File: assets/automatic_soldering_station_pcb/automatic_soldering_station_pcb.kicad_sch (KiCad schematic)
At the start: 25 parts, among them J1 XY_MOS, J2 MAX6675, J3 MAX6675, J4 MAX6675

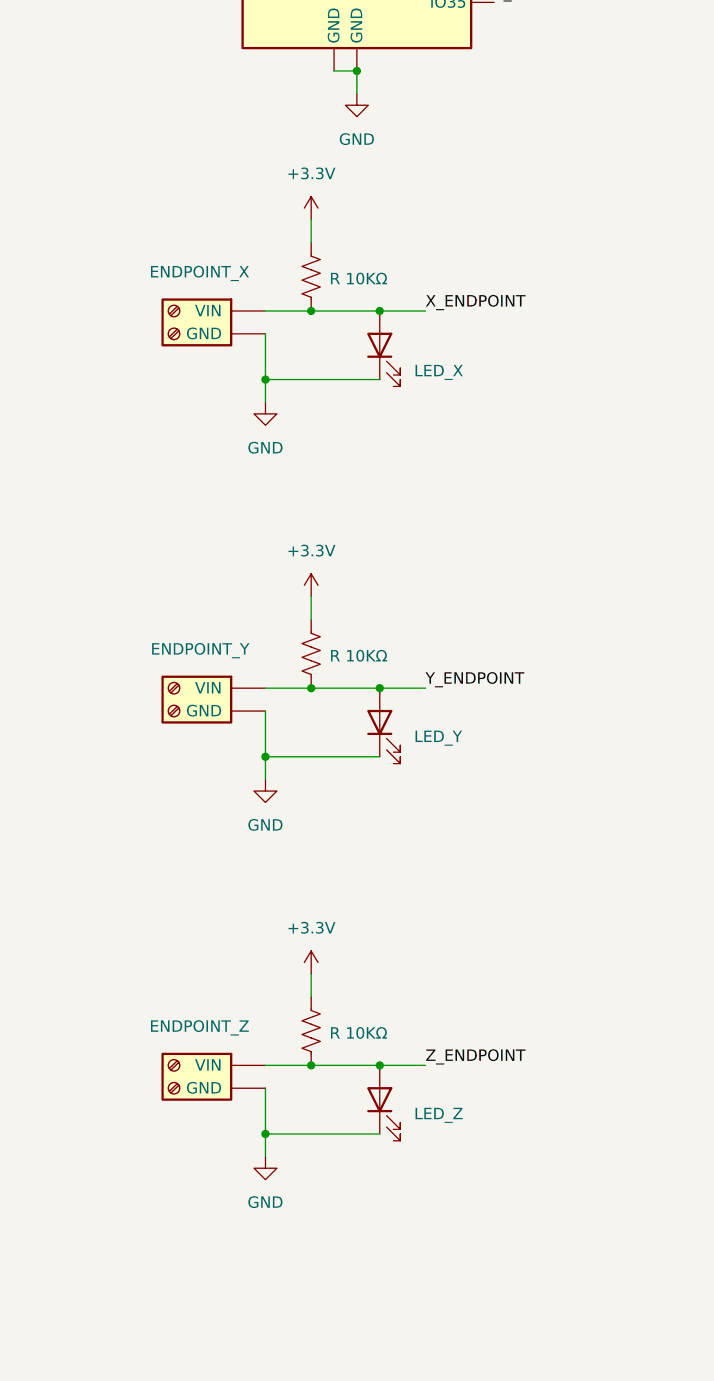
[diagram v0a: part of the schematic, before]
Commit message: pcb: add autorouted results
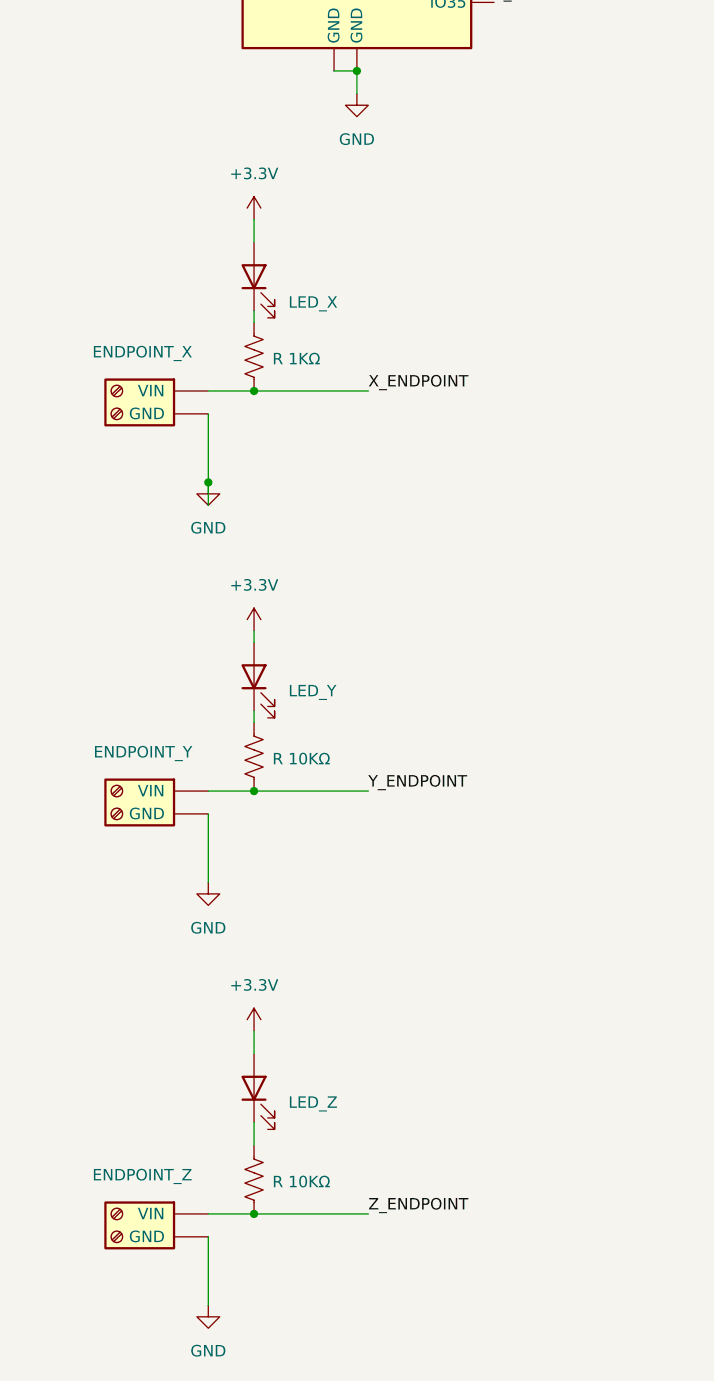
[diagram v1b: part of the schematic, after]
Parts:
- MOTOR_S_CONN1, MOTOR_X_CONN1, MOTOR_Y_CONN1, MOTOR_Z_CONN1: footprint Connector_JST:JST_PH_S4B-PH-K_1x04_P2.00mm_Horizontal -> Connector_JST:JST_PH_B4B-PH-K_1x04_P2.00mm_Vertical
- R1: value R 10KΩ -> R 1KΩ
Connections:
- net +3.3V: now also D1.2 (A), D2.2 (A), D3.2 (A); no longer R1.1, R2.1, R3.1
- net GND: no longer D1.1 (K), D2.1 (K), D3.1 (K)
- net X_ENDPOINT: no longer D1.2 (A)
- net Y_ENDPOINT: no longer D2.2 (A)
- net Z_ENDPOINT: no longer D3.2 (A)
- new net: D2.1 (K), R2.1
- new net: D1.1 (K), R1.1
- new net: D3.1 (K), R3.1

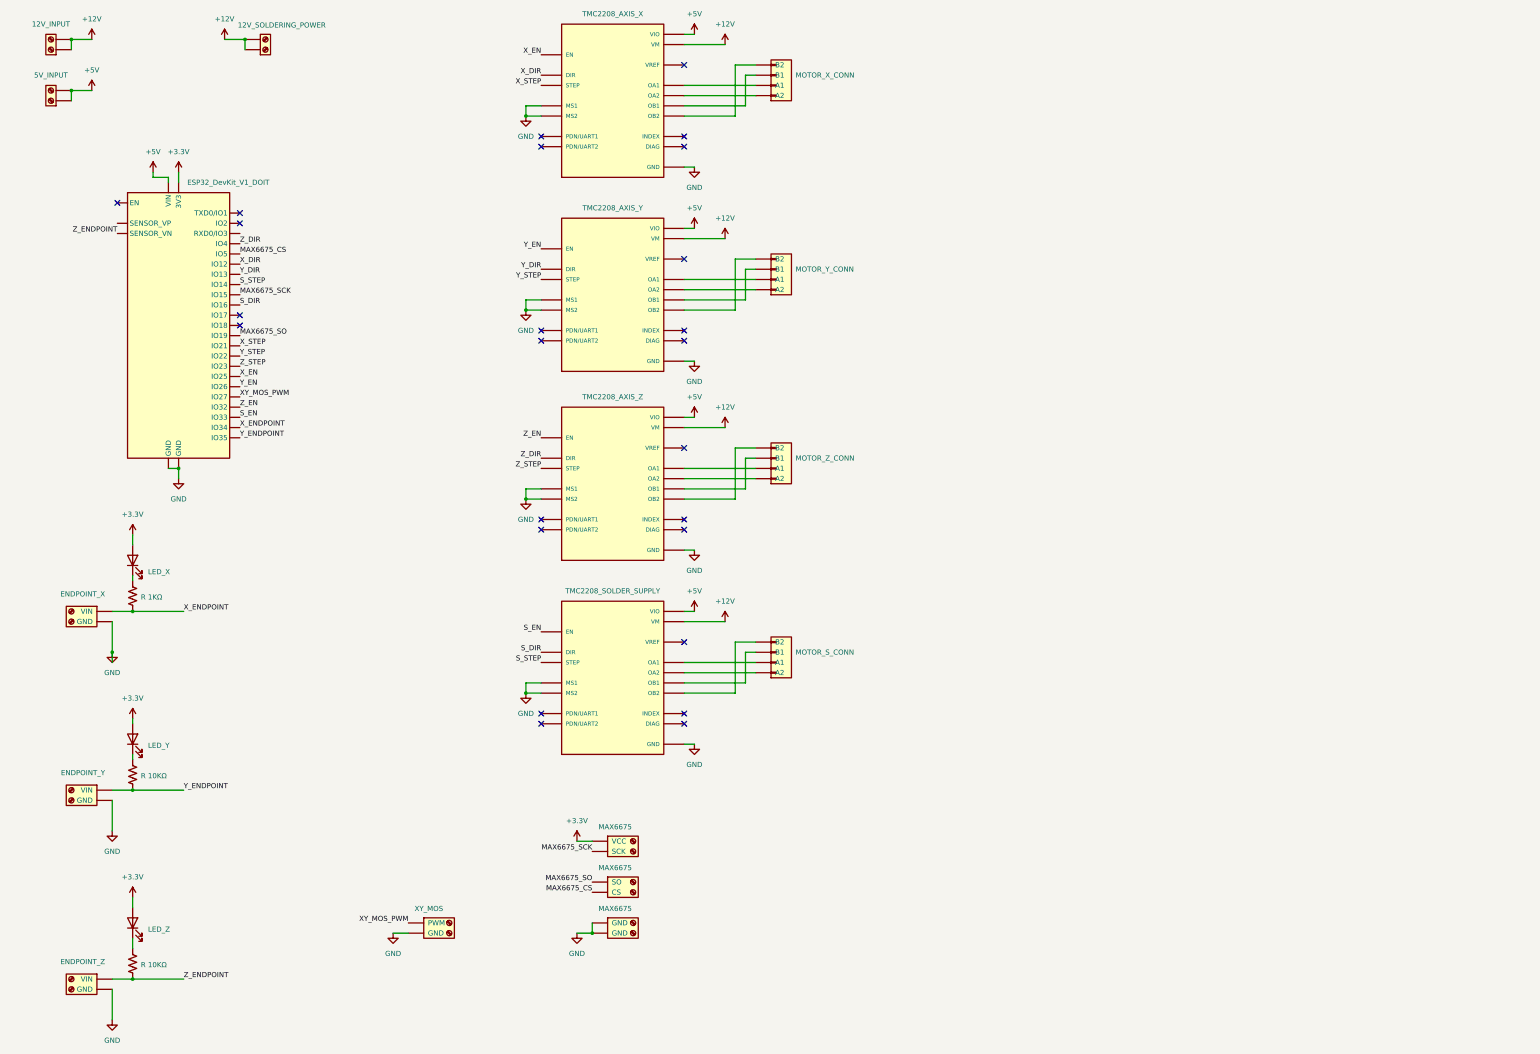
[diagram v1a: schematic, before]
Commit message: pcb: add buck converter and reroute pcb manually
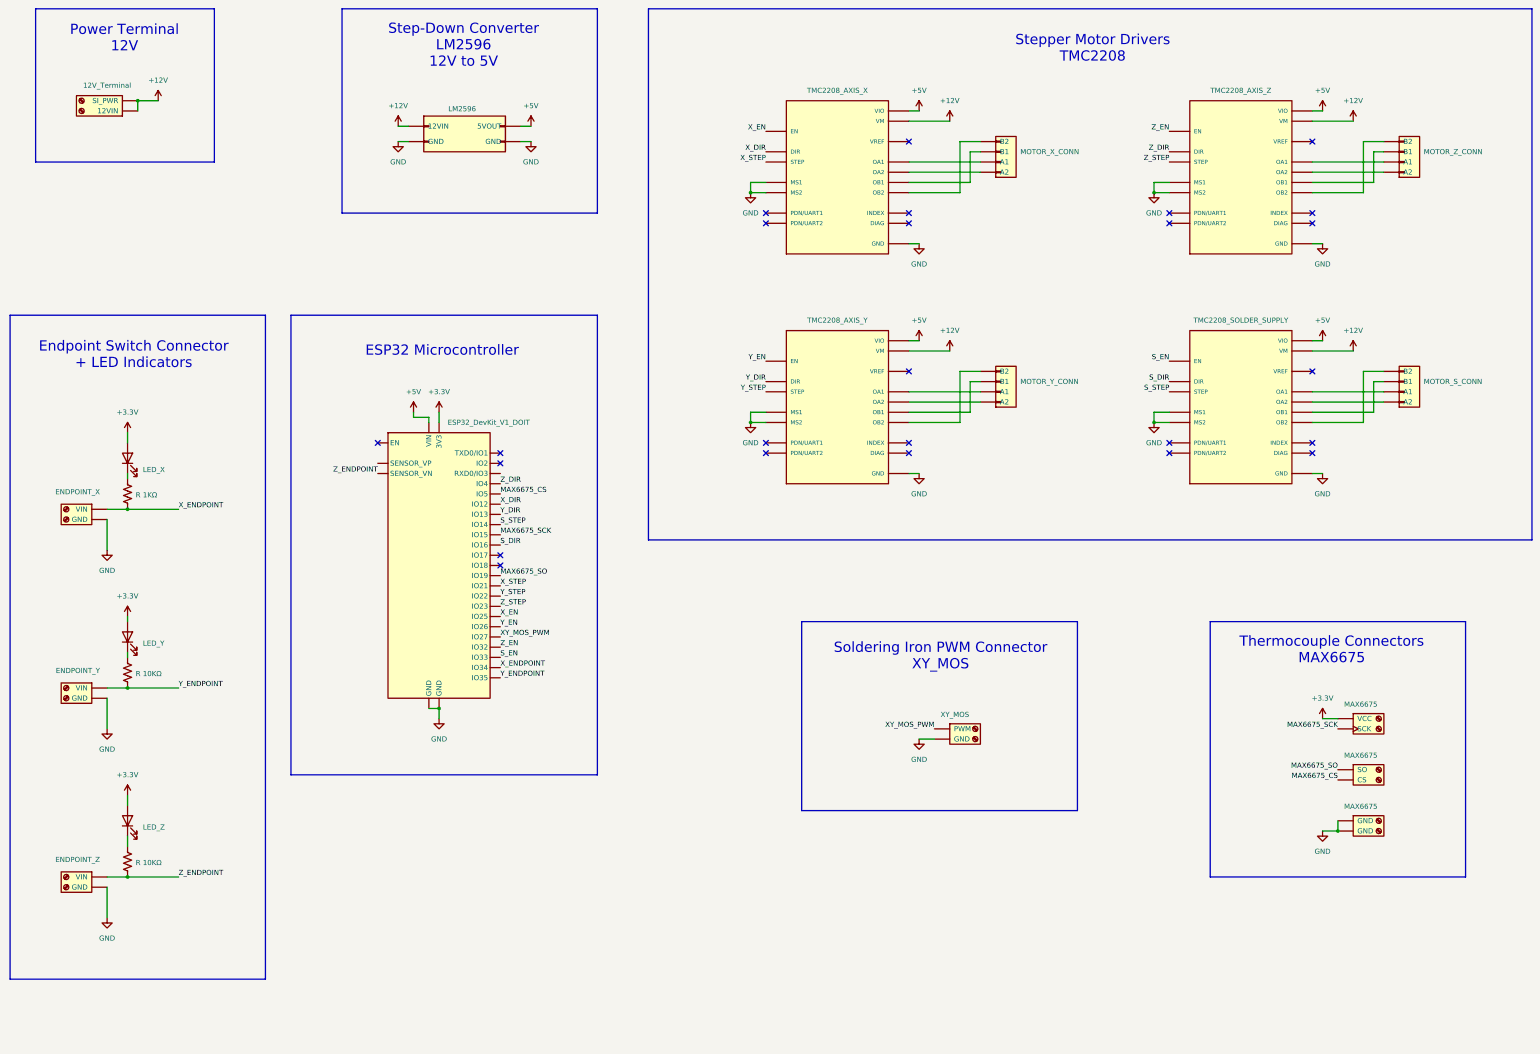
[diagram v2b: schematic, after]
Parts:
- removed 12V1: 12V_SOLDERING_POWER, TerminalBlock_MetzConnect:TerminalBlock_MetzConnect_Type055_RT01502HDWU_1x02_P5.00mm_Horizontal, symbol Connector:Screw_Terminal_01x02
- removed 5V1: 5V_INPUT, TerminalBlock_MetzConnect:TerminalBlock_MetzConnect_Type055_RT01502HDWU_1x02_P5.00mm_Horizontal, symbol Connector:Screw_Terminal_01x02
- added LM2596: LM2596, LM2596_Board:LM2596_Board, symbol LM2596:LM2596_Board
- 12V2: value 12V_INPUT -> 12V_Terminal
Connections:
- net +12V: now also LM2596.0 (12VIN)
- net +5V: now also LM2596.2 (5VOUT)
- net GND: now also LM2596.1 (GND), LM2596.3 (GND)
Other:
- note added: "ESP32 Microcontroller"
- note added: "Endpoint Switch Connector + LED Indicators"
- note added: "Power Terminal 12V"
- note added: "Soldering Iron PWM Connector XY_MOS"
- note added: "Step-Down Converter LM2596 12V to 5V"
- note added: "Stepper Motor Drivers TMC2208"
- note added: "Thermocouple Connectors MAX6675"

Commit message: pcb: add I2C terminal to schematic
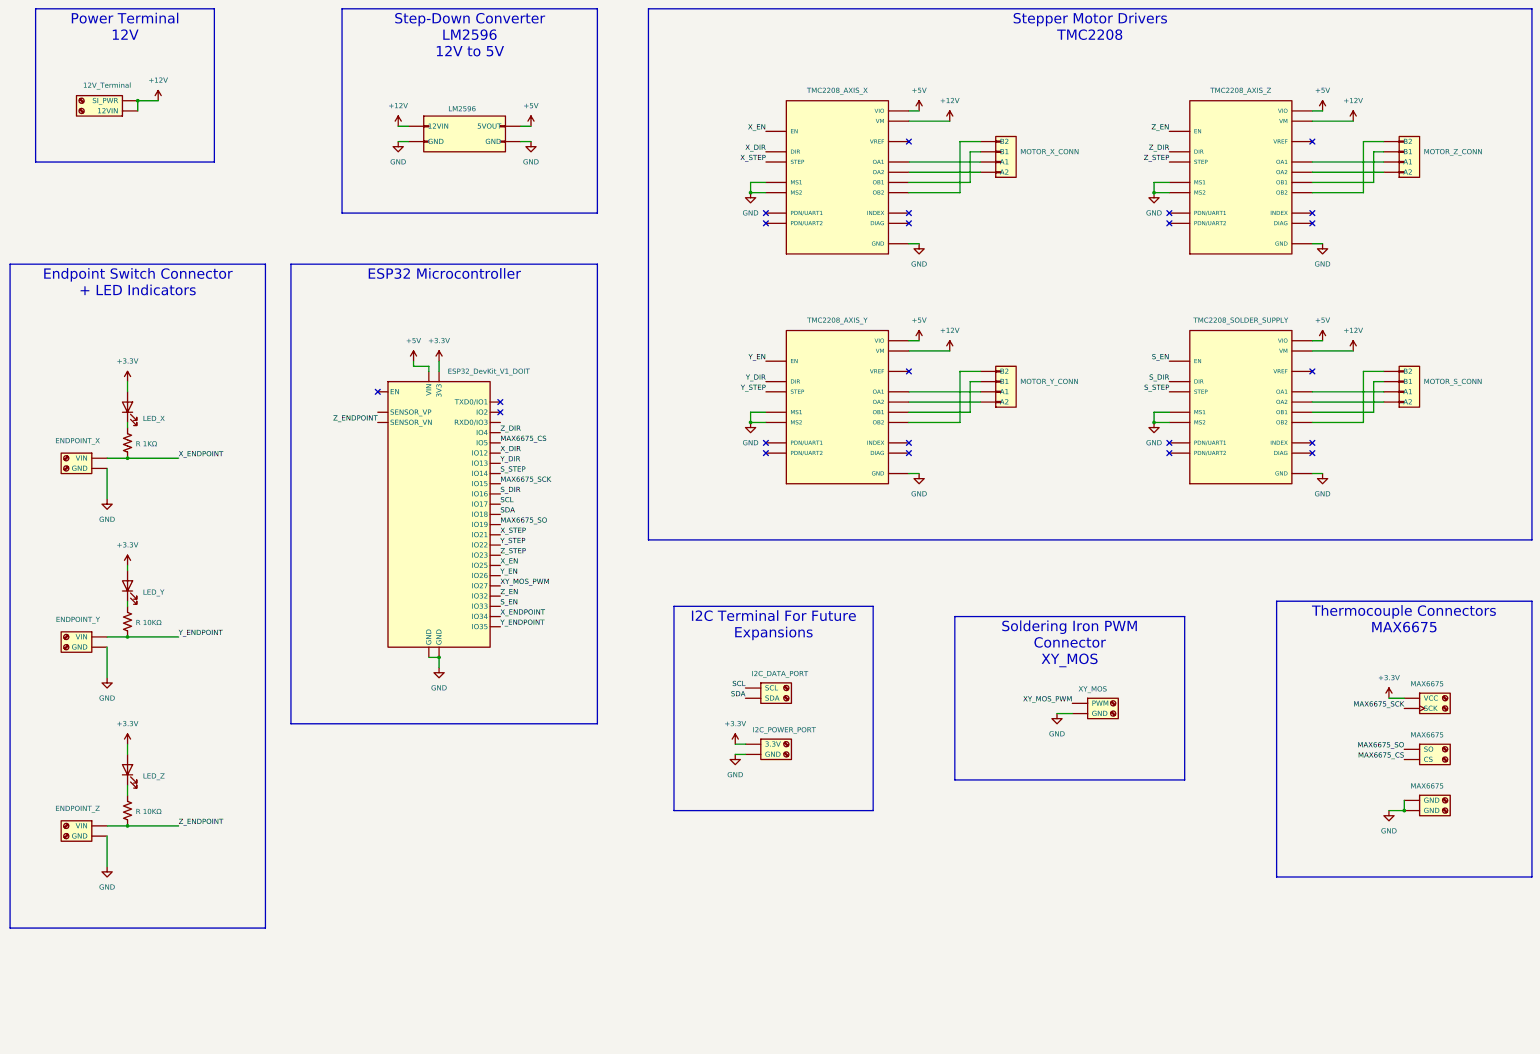
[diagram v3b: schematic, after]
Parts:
- added ENDPOINT_Y2: I2C_POWER_PORT, TerminalBlock_MetzConnect:TerminalBlock_MetzConnect_Type055_RT01502HDWU_1x02_P5.00mm_Horizontal, symbol Connector:Screw_Terminal_01x02
- added J5: I2C_DATA_PORT, TerminalBlock_MetzConnect:TerminalBlock_MetzConnect_Type055_RT01502HDWU_1x02_P5.00mm_Horizontal, symbol Connector:Screw_Terminal_01x02
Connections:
- net +3.3V: now also ENDPOINT_Y2.1 (3.3V)
- net GND: now also ENDPOINT_Y2.2 (GND)
- net SCL: now reaches ESP32_DevKit_V1_DOIT1.22 (IO17)
- net SCL: now also J5.1 (SCL)
- net SDA: now reaches ESP32_DevKit_V1_DOIT1.24 (IO18)
- net SDA: now also J5.2 (SDA)
- no-connect marks 25 -> 23
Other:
- note removed: "ESP32 Microcontroller"
- note removed: "Endpoint Switch Connector + LED Indicators"
- note removed: "Power Terminal 12V"
- note removed: "Soldering Iron PWM Connector XY_MOS"
- note removed: "Step-Down Converter LM2596 12V to 5V"
- note removed: "Stepper Motor Drivers TMC2208"
- note removed: "Thermocouple Connectors MAX6675"

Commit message: pcb: add pcb output files
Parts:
- R1: value R 1KΩ -> R 10KΩ
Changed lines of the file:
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@@
 			)
 		)
-		(property "Value" "R 1KΩ"
+		(property "Value" "R 10KΩ"
 			(at 50.292 133.604 0)
 			(effects
